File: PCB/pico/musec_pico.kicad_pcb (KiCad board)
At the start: 2 copper layers, 218 x 128.1 mm, 63 parts, among them J1 Pedal, J2 PJ313, J3 PJ313, SW1 SW_DIP_x01, SW2 SW_DIP_x01, SW3 SW_DIP_x01, SW4 SW_DIP_x01, SW5 SW_DIP_x01, SW6 SW_DIP_x01, SW7 SW_DIP_x01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

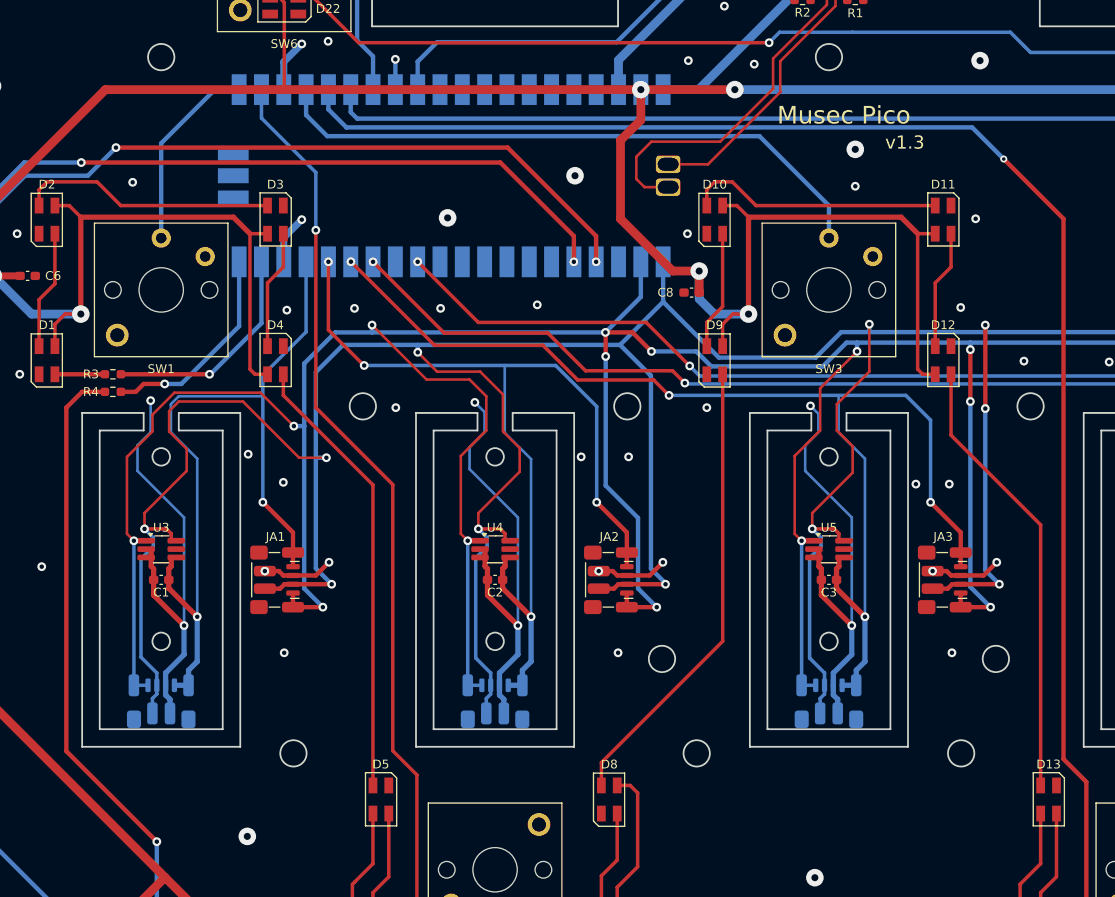
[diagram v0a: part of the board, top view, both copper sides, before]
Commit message: Explicit I2C Pull-ups
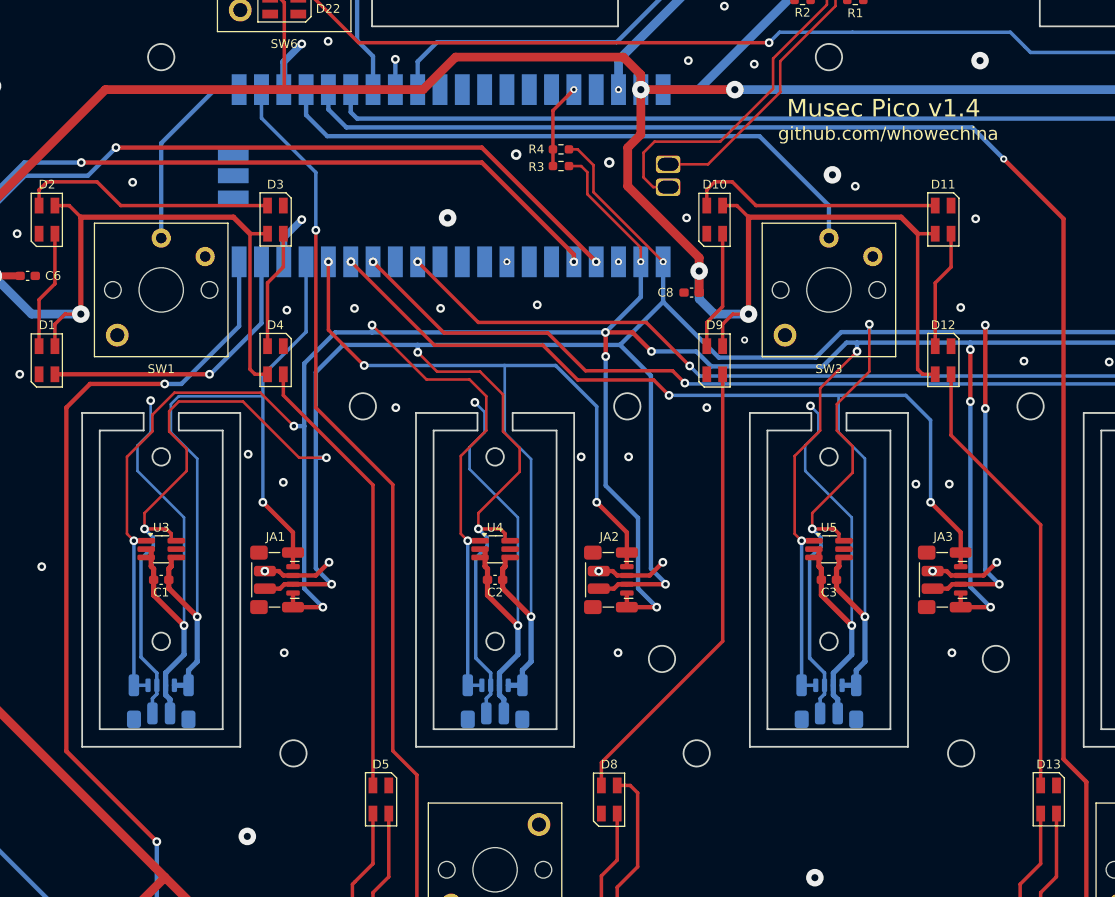
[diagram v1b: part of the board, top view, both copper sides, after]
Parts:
- R3, R4: value 10 -> 5K1
- moved R4 58.0 mm to (183.7, 96.1)
- moved R3 56.2 mm to (183.7, 98.0), turned to 180 degrees
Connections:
- R3 pad 1: Net-(D1-In) -> /SCL
- R3 pad 2: Net-(U1-GPIO14) -> +3V3
- R4 pad 1: Net-(U1-GPIO15) -> /SDA
- R4 pad 2: Net-(J1-Pin_2) -> +3V3
- U1 pad 19: Net-(U1-GPIO14) -> Net-(D1-In)
- U1 pad 20: Net-(U1-GPIO15) -> Net-(J1-Pin_2)
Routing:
- net Net-(D1-In): track 5.69 -> 32.9 mm, vias 0 -> 1
- net Net-(J1-Pin_2): track 76.4 -> 102.1 mm, vias 2 -> 3
- net Net-(U1-GPIO14): track 25.4 -> 0.00 mm, vias 1 -> 0
- net Net-(U1-GPIO15): track 23.9 -> 0.00 mm, vias 1 -> 0
- net /SDA: track 628.2 -> 646.0 mm, vias 19 -> 20
- net /SCL: track 583.4 -> 598.5 mm, vias 22 -> 23
- net +3V3: track 0.00 -> 9.69 mm, vias 0 -> 1
- net Net-(J1-Pin_3): track 193.3 -> 191.6 mm
- net +5V: track 781.3 -> 782.9 mm
- net Net-(U1-USB2): track 44.3 -> 42.8 mm
- net Net-(J2-T): track 391.3 -> 390.1 mm
- net GND: vias 87 -> 92
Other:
- board text added: "Musec Pico v1.4"
- board text added: "github.com/whowechina"
- board text removed: "Musec Pico"
- board text removed: "v1.3"
